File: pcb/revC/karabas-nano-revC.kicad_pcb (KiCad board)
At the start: 2 copper layers, 101.6 x 99.7 mm, 157 parts, among them J1 DC 5V, J10 PWR, J11 AVR ISP, J2 TAPE IN/OUT, J3 A/V, J4 BUS, J5 KEYBOARD, J6 BUS, J7 JTAG, J8 KEYBOARD, J9 RGB, Q1 BC846B, SW1 RESET, SW10 8, SW11 9, SW12 0, SW13 Q, SW14 A, SW15 CS, SW16 W, SW17 S, SW18 Z, SW19 E, SW2 NMI, SW20 D, SW21 X, SW22 R, SW23 F, SW24 C, SW25 T, SW26 G, SW27 V, SW28 Y, SW29 H, SW3 1, SW30 B, SW31 U, SW32 J, SW33 N, SW34 I, SW35 K, SW36 M, SW37 O, SW38 L, SW39 SS, SW4 2, SW40 P, SW41 Enter, SW42 Space, SW5 3, SW6 4, SW7 5, SW8 6, SW9 7, U1 Z80, U13 LM1117-3.3, U2 27C512, U3 BS62LV1600, U4 ATmega8A-AU, U6 EPM3256ATC144, U7 MicroSD, U9 AD724, Y1 28MHz, Y2 XMHz, Y3 4.43MHz, Y4 20MHz

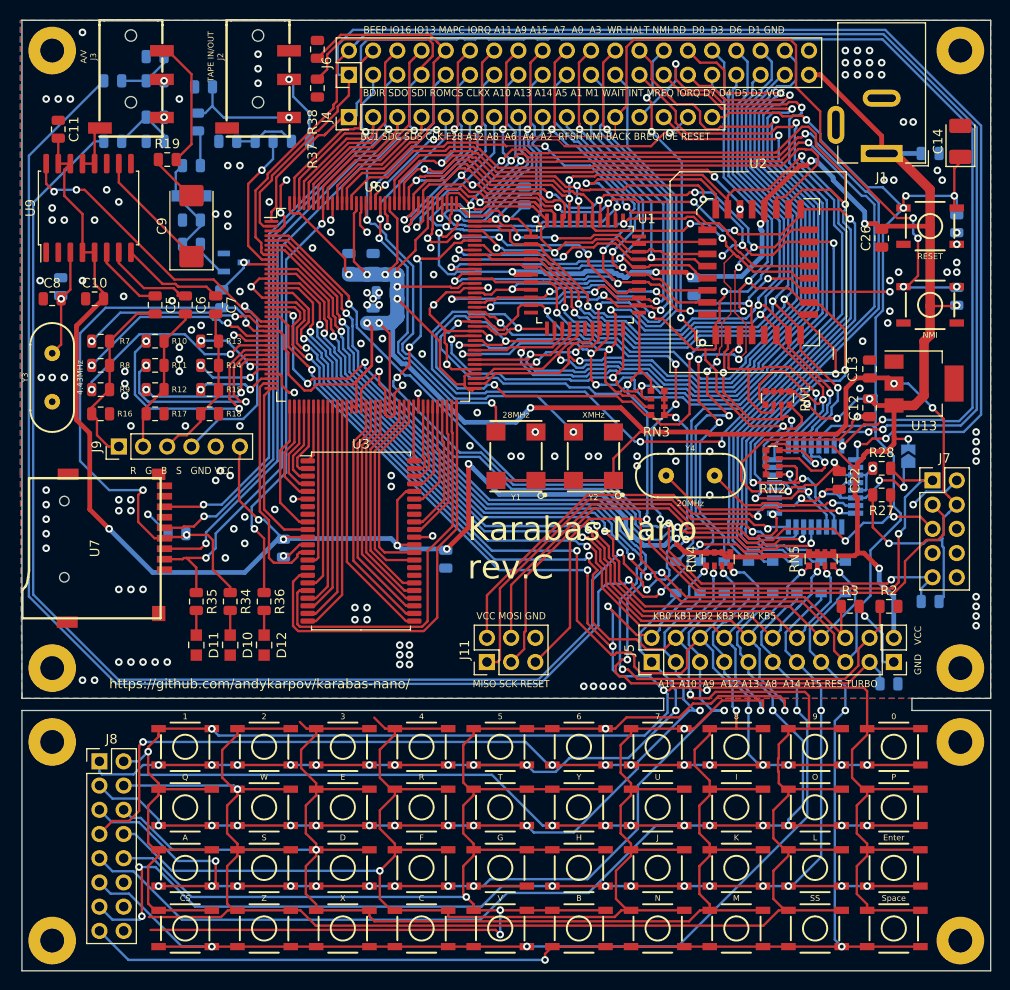
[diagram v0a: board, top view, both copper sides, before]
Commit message: Fixed PLCC32 footprint
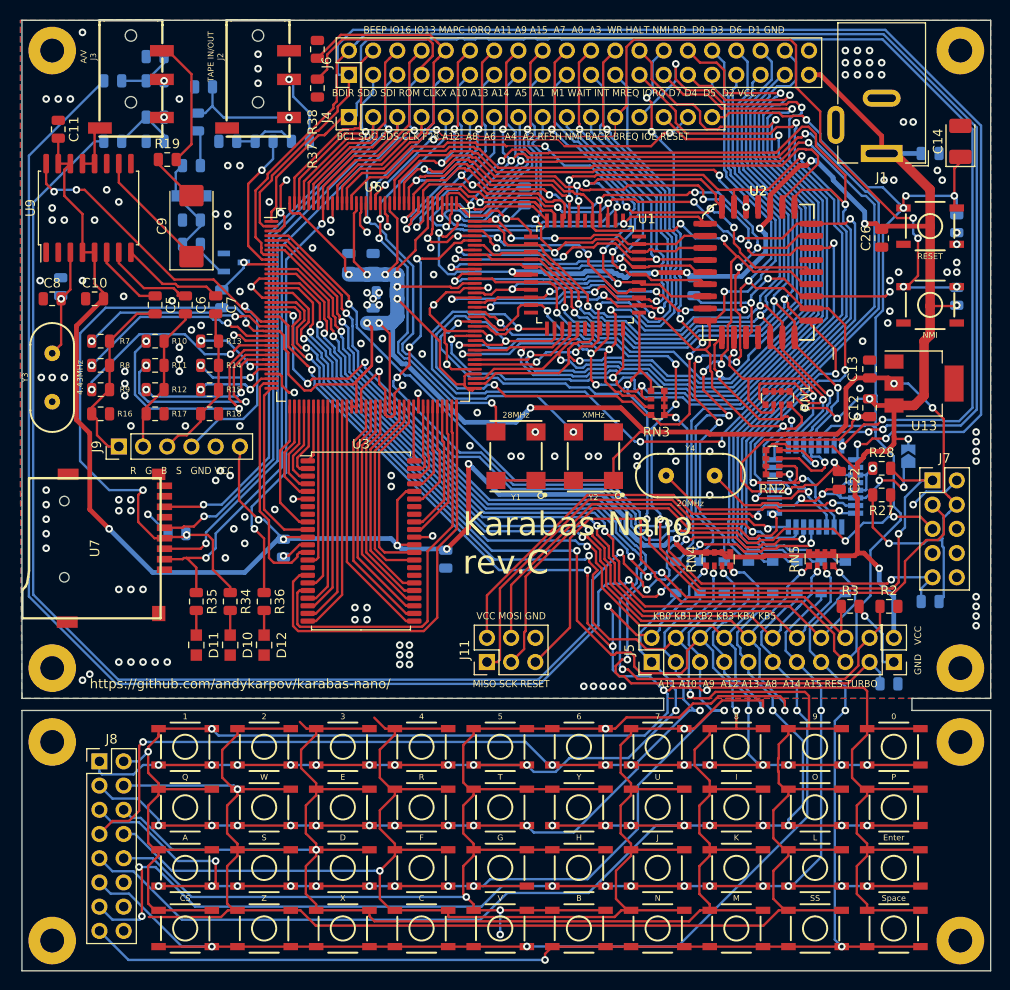
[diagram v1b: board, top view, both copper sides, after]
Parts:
- removed the U2 at (166.1, 77.2)
- added U2: 27C512, footprints:PLCC-32_11.4x14.0mm_P1.27mm-bigpads, F.Cu at (166.1, 77.2)
- added U2: 27C512, Package_LCC:PLCC-32_11.4x14.0mm_P1.27mm, F.Cu at (166.1, 77.2)
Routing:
- net /KA13: track 182.0 -> 136.4 mm
- net /KB4: track 266.0 -> 229.2 mm
- net /A11: track 118.4 -> 116.3 mm, vias 8 -> 7
- net /D2: track 97.7 -> 95.6 mm
- net /~ROMCS: track 58.3 -> 59.8 mm, vias 2 -> 4
- net /A10: track 106.2 -> 107.3 mm
- net /ROM_A14: track 61.8 -> 60.8 mm
- net /A8: track 117.6 -> 116.8 mm
- net GND: track 192.9 -> 193.6 mm
- net /D0: track 91.0 -> 91.7 mm
- net /D3: track 96.6 -> 96.0 mm
- net /A6: track 53.2 -> 52.7 mm
- net /A1: track 57.5 -> 57.0 mm
- net /A0: track 61.8 -> 61.3 mm
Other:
- board text added: "BDIR SDO SDI ROM CLKX A10 A13 A14 A5 A1 M1 WAIT INT MREQ IORQ D7 D4 D5 D2 VCC"
- board text removed: "BDIR SDO SDI ROMCS CLKX A10 A13 A14 A5 A1 M1 WAIT INT MREQ IORQ D7 D4 D5 D2 VCC"
